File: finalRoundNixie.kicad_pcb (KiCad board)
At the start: 2 copper layers, 37 x 56.3 mm, 60 parts, among them J1 Conn_01x06_Male, J2 HV_IN, J3 Conn_01x06_Female, J4 HV_OUT, Q1 MMBTA42LT1, Q10 MMBTA42LT1, Q11 AO3400, Q12 AO3400, Q13 AO3400, Q14 MMBTA42LT1, Q15 MMBTA42LT1, Q2 MMBTA42LT1, Q3 MMBTA42LT1, Q4 MMBTA42LT1, Q5 MMBTA42LT1, Q6 MMBTA42LT1, Q7 MMBTA42LT1, Q8 MMBTA42LT1, Q9 MMBTA42LT1, U1 74HC595D, U2 nixie-tube, U3 74HC595D, U4 ams1117-5.0

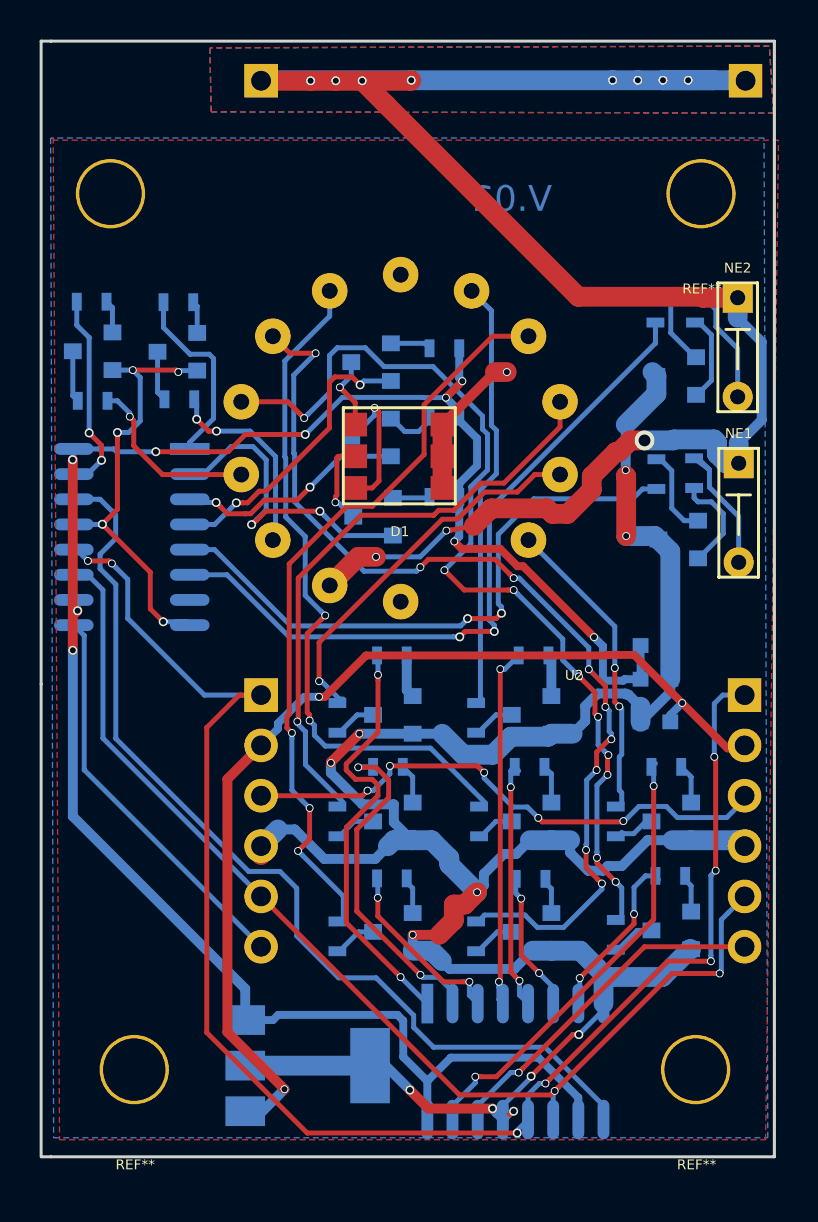
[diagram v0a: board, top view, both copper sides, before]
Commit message: changed AO3400 pin position (2 board)
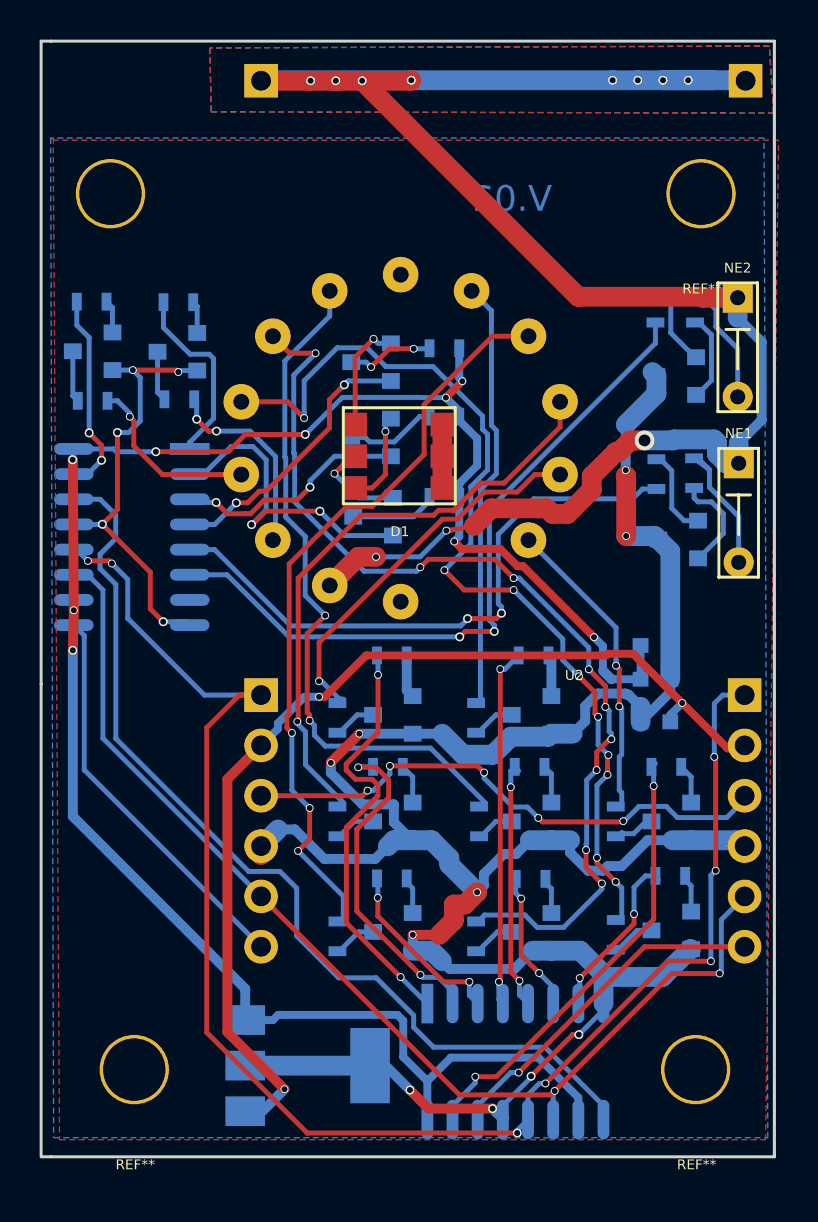
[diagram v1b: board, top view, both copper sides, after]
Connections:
- Q11 pad 1: Net-(Q11-Pad1) -> Net-(D1-Pad2)
- Q11 pad 3: Net-(D1-Pad2) -> Net-(Q11-Pad3)
- Q12 pad 1: Net-(Q12-Pad1) -> Net-(D1-Pad3)
- Q12 pad 3: Net-(D1-Pad3) -> Net-(Q12-Pad3)
- Q13 pad 1: Net-(Q13-Pad1) -> Net-(D1-Pad4)
- Q13 pad 3: Net-(D1-Pad4) -> Net-(Q13-Pad3)
- R11 pad 2: Net-(Q11-Pad1) -> Net-(Q11-Pad3)
- R12 pad 2: Net-(Q12-Pad1) -> Net-(Q12-Pad3)
- R13 pad 2: Net-(Q13-Pad1) -> Net-(Q13-Pad3)
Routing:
- net GND: track 154.6 -> 149.4 mm, vias 17 -> 15
- net Net-(Q12-Pad3): track 0.00 -> 4.62 mm
- net Net-(Q11-Pad3): track 0.00 -> 4.50 mm
- net Net-(Q13-Pad3): track 0.00 -> 4.45 mm, vias 0 -> 2
- net Net-(Q12-Pad1): track 2.65 -> 0.00 mm
- net Net-(D1-Pad3): track 7.14 -> 4.79 mm
- net Net-(Q13-Pad1): track 2.05 -> 0.00 mm
- net Net-(D1-Pad4): track 3.71 -> 5.68 mm
- net Net-(Q11-Pad1): track 1.87 -> 0.00 mm
- net /Blue: track 15.0 -> 14.2 mm
- net +5V: track 103.4 -> 102.7 mm

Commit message: remove silkscreen on female pins, re routed some of the tracks
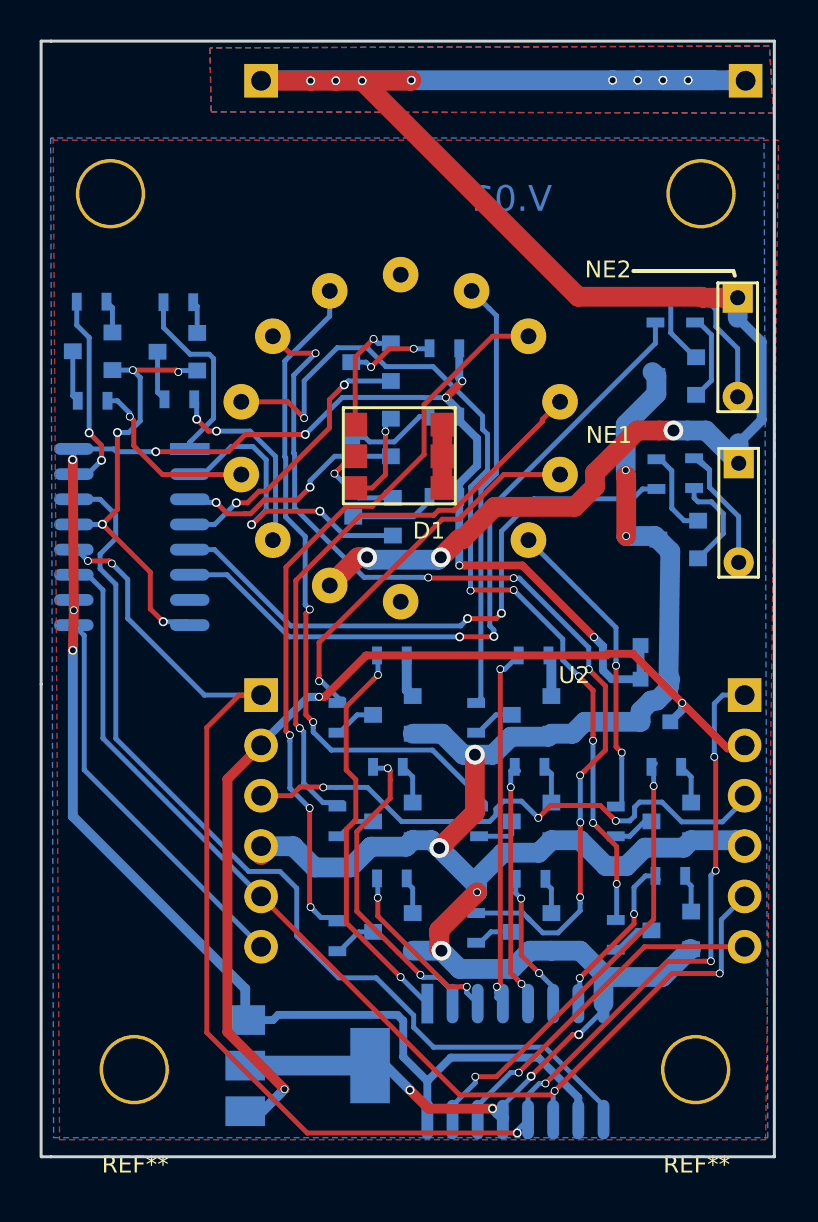
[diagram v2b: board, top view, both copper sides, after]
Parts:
- J2: footprint Socket_Strips:Socket_Strip_Angled_1x01_Pitch2.54mm -> nixie-tube-fp:Socket_Strip_Angled_1x01_Pitch2.54mm_without_silk
- J3: footprint Socket_Strips:Socket_Strip_Angled_1x06_Pitch2.54mm -> nixie-tube-fp:Socket_Strip_Angled_1x06_Pitch2.54mm_without_silk
- moved R4 0.42 mm to (173.4, 85.0)
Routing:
- net GND: track 149.4 -> 139.9 mm
- net Net-(R3-Pad1): track 48.4 -> 46.8 mm, vias 9 -> 7
- net /s1: track 21.8 -> 20.4 mm
- net /s2: track 17.2 -> 15.9 mm
- net /PWREN: track 27.6 -> 28.5 mm, vias 5 -> 3
- net /n4: track 1.58 -> 2.35 mm
- net Net-(R5-Pad1): track 34.7 -> 34.1 mm
- net Net-(R4-Pad1): track 49.6 -> 49.0 mm, vias 9 -> 7
- net /n9: track 1.79 -> 2.39 mm
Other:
- board text added: "HV"

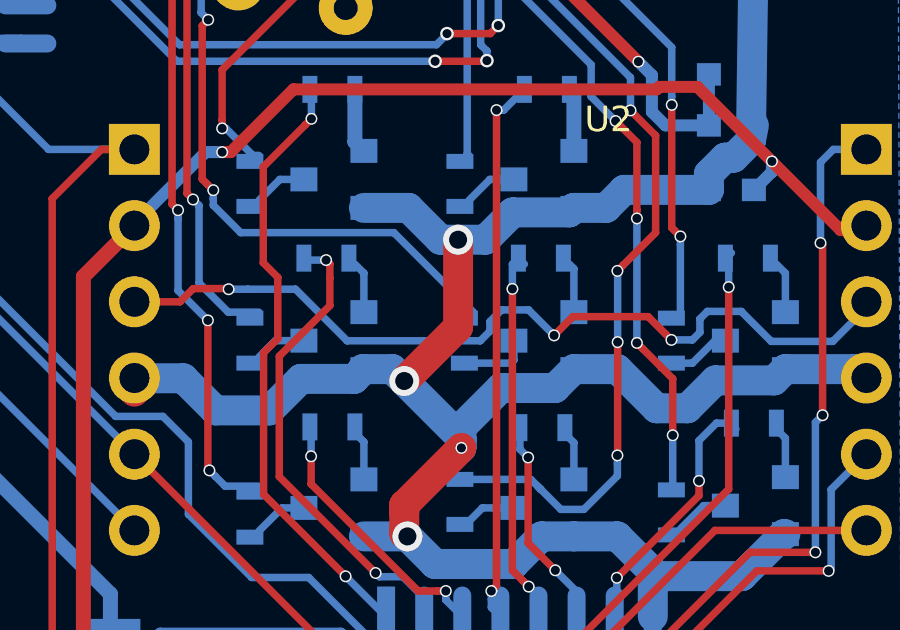
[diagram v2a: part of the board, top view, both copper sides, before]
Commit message: fixed some badly routed tracks
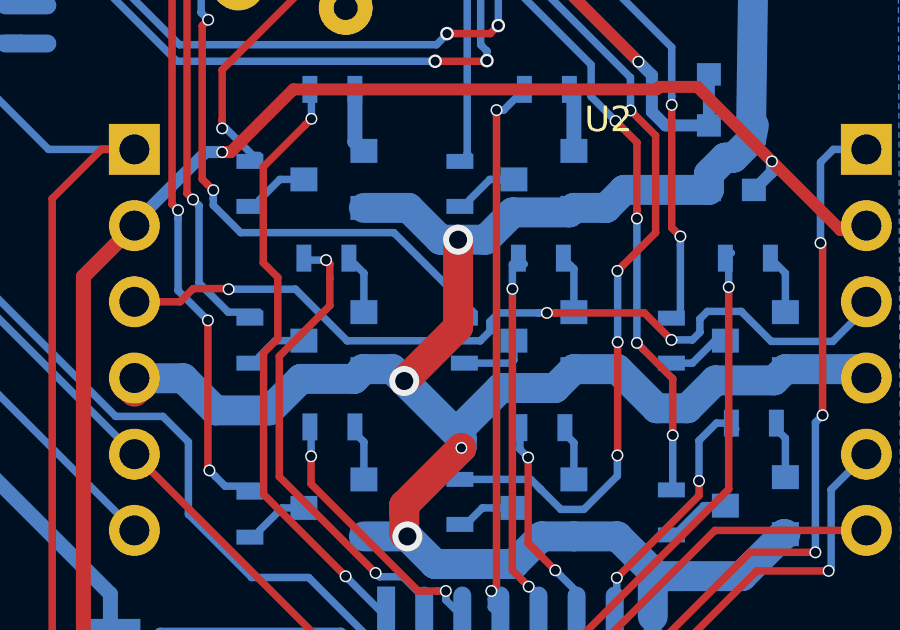
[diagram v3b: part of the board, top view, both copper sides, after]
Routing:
- net /PWREN: track 28.5 -> 27.9 mm
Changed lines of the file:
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@@
     (links 108)
     (no_connects 0)
-    (area 151.424999 40.224999 188.575001 96.675001)
+    (area 141.050001 40.224999 208.899524 100.700001)
     (thickness 1.6)
     (drawings 17)
-    (tracks 840)
+    (tracks 838)
     (zones 0)
     (modules 60)
@@
   (segment (start 185.824999 84.635001) (end 187 83.46) (width 0.25) (layer B.Cu) (net 7) (status 20))
   (via (at 185.74 87.35) (size 0.4) (drill 0.3) (layers F.Cu B.Cu) (net 7))
-  (segment (start 176.589998 79.5) (end 175.739998 78.65) (width 0.25) (layer B.Cu) (net 8))
-  (segment (start 174.45 79.360002) (end 174.130002 79.68) (width 0.25) (layer B.Cu) (net 8))
-  (segment (start 175.739998 78.65) (end 174.839998 78.65) (width 0.25) (layer B.Cu) (net 8))
-  (segment (start 174.130002 79.68) (end 169.690002 79.68) (width 0.25) (layer B.Cu) (net 8))
-  (segment (start 174.839998 78.65) (end 174.45 79.039998) (width 0.25) (layer B.Cu) (net 8))
-  (segment (start 174.45 79.039998) (end 174.45 79.360002) (width 0.25) (layer B.Cu) (net 8))
-  (segment (start 169.690002 79.68) (end 167.970002 77.96) (width 0.25) (layer B.Cu) (net 8))
-  (segment (start 167.970002 77.96) (end 166.38 77.96) (width 0.25) (layer B.Cu) (net 8))
-  (segment (start 166.38 77.96) (end 165.74 77.96) (width 0.25) (layer B.Cu) (net 8))
+  (segment (start 176.632842 78.75) (end 176.35 78.75) (width 0.25) (layer F.Cu) (net 8))
+  (segment (start 179.6 78.75) (end 176.632842 78.75) (width 0.25) (layer F.Cu) (net 8))
+  (segment (start 180.5 79.65) (end 179.6 78.75) (width 0.25) (layer F.Cu) (net 8))
+  (segment (start 176.067158 78.75) (end 176.35 78.75) (width 0.25) (layer B.Cu) (net 8))
+  (segment (start 174.45 79.360002) (end 174.45 79.039998) (width 0.25) (layer B.Cu) (net 8))
+  (segment (start 174.130002 79.68) (end 174.45 79.360002) (width 0.25) (layer B.Cu) (net 8))
+  (segment (start 169.690002 79.68) (end 174.130002 79.68) (width 0.25) (layer B.Cu) (net 8))
+  (segment (start 167.970002 77.96) (end 169.690002 79.68) (width 0.25) (layer B.Cu) (net 8))
+  (segment (start 174.739998 78.75) (end 176.067158 78.75) (width 0.25) (layer B.Cu) (net 8))
+  (segment (start 174.45 79.039998) (end 174.739998 78.75) (width 0.25) (layer B.Cu) (net 8))
+  (segment (start 165.74 77.96) (end 167.970002 77.96) (width 0.25) (layer B.Cu) (net 8))
+  (via (at 176.35 78.75) (size 0.4) (drill 0.3) (layers F.Cu B.Cu) (net 8))
   (segment (start 164.12 78.38) (end 164.56 77.94) (width 0.25) (layer F.Cu) (net 8))
   (segment (start 164.56 77.94) (end 165.72 77.94) (width 0.25) (layer F.Cu) (net 8))
@@
   (segment (start 181.45 78.95) (end 181.7 78.7) (width 0.25) (layer B.Cu) (net 8))
   (segment (start 183.827854 79.7) (end 185.88 79.7) (width 0.25) (layer B.Cu) (net 8))
-  (segment (start 180.300001 79.450001) (end 180.5 79.65) (width 0.25) (layer F.Cu) (net 8))
-  (segment (start 177.215 78.874998) (end 179.724998 78.874998) (width 0.25) (layer F.Cu) (net 8))
-  (segment (start 176.589998 79.5) (end 177.215 78.874998) (width 0.25) (layer F.Cu) (net 8))
-  (segment (start 179.724998 78.874998) (end 180.300001 79.450001) (width 0.25) (layer F.Cu) (net 8))
   (via (at 180.5 79.65) (size 0.4) (drill 0.3) (layers F.Cu B.Cu) (net 8))
-  (via (at 176.589998 79.5) (size 0.4) (drill 0.3) (layers F.Cu B.Cu) (net 8))
   (via (at 167.95 66.35) (size 1) (drill 0.6) (layers F.Cu B.Cu) (net 9))
   (segment (start 168.07 66.47) (end 171.55 66.47) (width 1) (layer B.Cu) (net 9))

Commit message: finalized every component and generated gerber file
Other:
- board text added: "GND"
- board text added: "MISO"
- board text added: "MOSI"
- board text added: "PWREN"
- board text added: "SCK"
- board text added: "STORE"
- board text added: "VDC"
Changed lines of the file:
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@@
     (area 141.050001 40.224999 208.899524 100.700001)
     (thickness 1.6)
-    (drawings 17)
+    (drawings 24)
     (tracks 838)
     (zones 0)
@@
     (40 Dwgs.User user)
     (41 Cmts.User user)
-    (42 Eco1.User user hide)
+    (42 Eco1.User user)
     (43 Eco2.User user hide)
     (44 Edge.Cuts user)
@@
     (visible_elements 7FFEFFFF)
     (pcbplotparams
-      (layerselection 0x3d4fc_80000001)
+      (layerselection 0x3d0fc_80000001)
       (usegerberextensions true)
       (usegerberattributes true)
@@
       (net 59 "Net-(NE2-Pad2)"))
   )
+  (gr_text MISO (at 168 86.25) (layer F.SilkS)
+    (effects (font (size 1.5 1.5) (thickness 0.3)))
+  )
+  (gr_text MOSI (at 181.73 86.49) (layer F.SilkS)
+    (effects (font (size 1.5 1.5) (thickness 0.3)))
+  )
+  (gr_text SCK (at 174.16 83.5) (layer F.SilkS)
+    (effects (font (size 1.5 1.5) (thickness 0.3)))
+  )
+  (gr_text GND (at 174.16 81.09) (layer F.SilkS)
+    (effects (font (size 1.5 1.5) (thickness 0.3)))
+  )
+  (gr_text PWREN (at 174.16 78.49) (layer F.SilkS)
+    (effects (font (size 1.5 1.5) (thickness 0.3)))
+  )
+  (gr_text VDC (at 174.21 75.84) (layer F.SilkS)
+    (effects (font (size 1.5 1.5) (thickness 0.3)))
+  )
+  (gr_text STORE (at 173.78 73.29) (layer F.SilkS)
+    (effects (font (size 1.5 1.5) (thickness 0.3)))
+  )
   (gr_text HV (at 174.5 42.33) (layer B.SilkS)

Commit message: finalized tracks and added symbols
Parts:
- moved R18 0.18 mm to (169.1, 77.1)
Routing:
- net GND: track 139.9 -> 177.7 mm, vias 15 -> 18
- net +5V: track 103.0 -> 122.0 mm, vias 9 -> 10
- net Net-(J2-Pad1): track 91.9 -> 86.4 mm, vias 11 -> 10
- net /SCK: track 56.3 -> 60.1 mm
- net +VDC: track 51.6 -> 54.8 mm
- net /DotU: track 30.4 -> 28.3 mm
- net Net-(R5-Pad1): track 34.1 -> 36.1 mm
- net Net-(R9-Pad1): track 19.2 -> 21.0 mm
- net Net-(R2-Pad1): track 9.34 -> 8.64 mm
- net /s8: track 10.8 -> 10.2 mm
- net Net-(R7-Pad1): track 38.1 -> 38.6 mm

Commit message: finalized everything and ready to send out
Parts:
- added Z?: skull, nixie-tube-fp:skull, F.Cu at (168.6, 42.9)
- added Z?: lightning, nixie-tube-fp:lightning, F.Cu at (182.4, 42.5)
- added Z?: skull, nixie-tube-fp:skull, B.Cu at (168.3, 42.8)
- added Z?: lightning, nixie-tube-fp:lightning, B.Cu at (182.3, 42.5)
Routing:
- net Net-(J2-Pad1): track 86.4 -> 89.1 mm

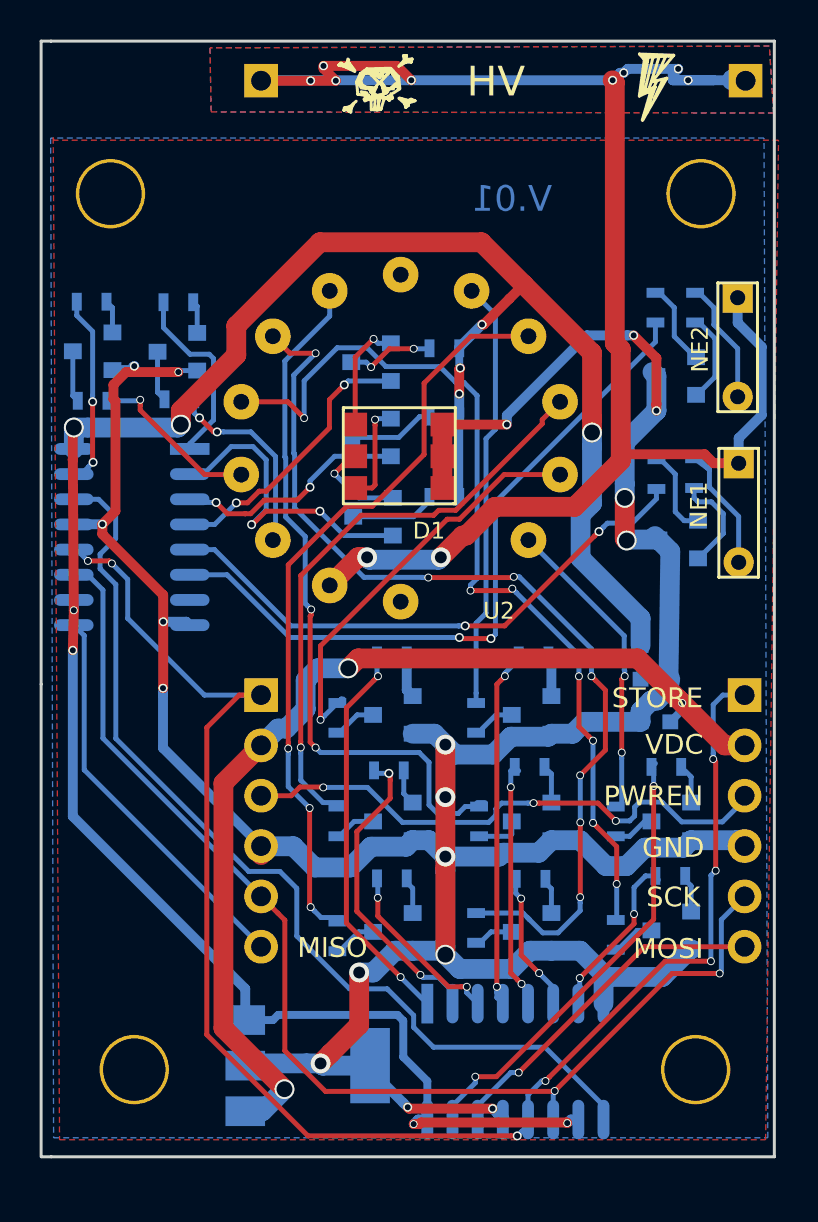
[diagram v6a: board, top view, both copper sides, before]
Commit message: fixed various bugs
RGB led not connected properly to the mosfet
AO3400 pin orientation is not same with datasheet
move silkscreen away on neon footprint
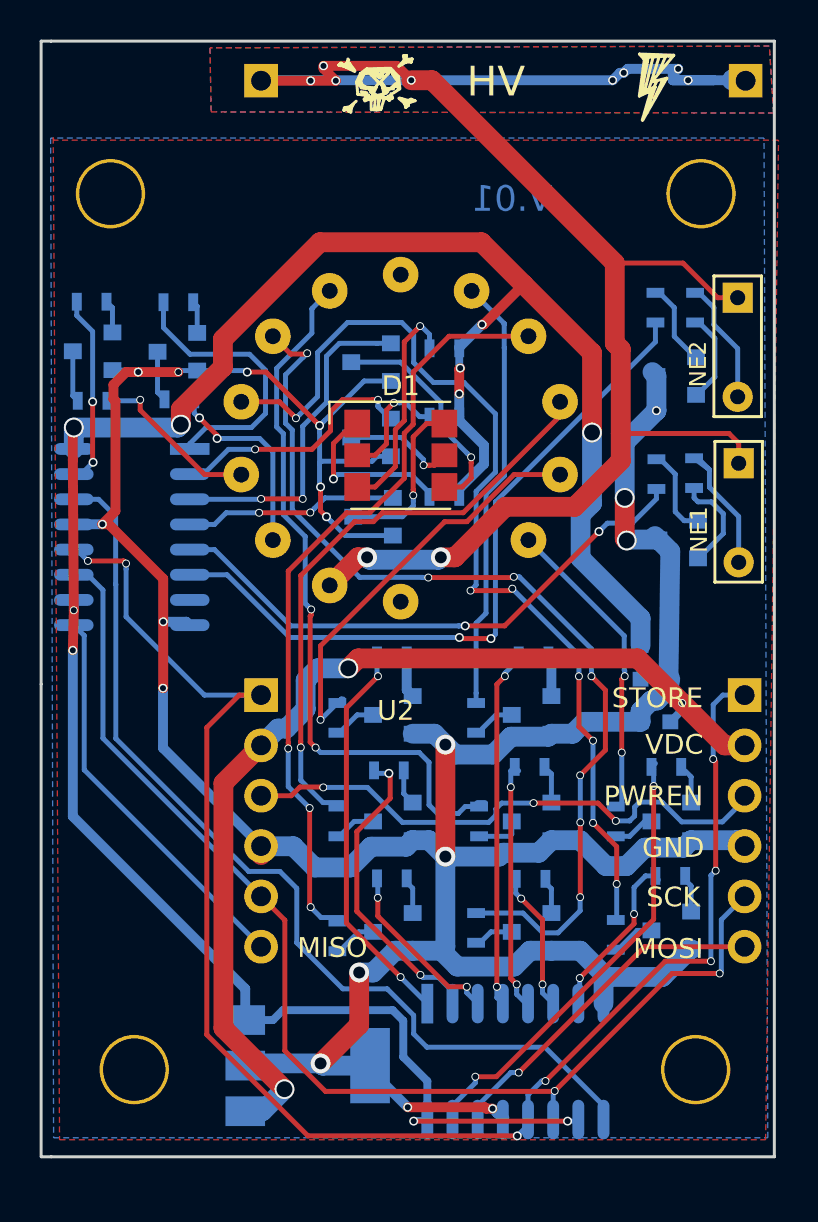
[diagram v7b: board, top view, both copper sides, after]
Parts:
- D1: value LED_CRGB -> LED_RGB_BGR; footprint nixie-tube-fp:Rgb-Led -> nixie-tube-fp:LED_RGB_5050-6
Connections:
- D1 pad 1: GND -> Net-(D1-Pad1)
- Q11 pad 1: Net-(D1-Pad2) -> /Blue
- Q11 pad 2: /Red -> GND
- Q11 pad 3: Net-(Q11-Pad3) -> Net-(D1-Pad6)
- Q12 pad 1: Net-(D1-Pad3) -> /Red
- Q12 pad 2: /Green -> GND
- Q12 pad 3: Net-(Q12-Pad3) -> Net-(D1-Pad5)
- Q13 pad 1: Net-(D1-Pad4) -> /Green
- Q13 pad 2: /Blue -> GND
- Q13 pad 3: Net-(Q13-Pad3) -> Net-(D1-Pad4)
- R11 pad 2: Net-(Q11-Pad3) -> Net-(D1-Pad1)
- R12 pad 2: Net-(Q12-Pad3) -> Net-(D1-Pad2)
- R13 pad 2: Net-(Q13-Pad3) -> Net-(D1-Pad3)
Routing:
- net Net-(D1-Pad1): track 0.00 -> 9.13 mm, vias 0 -> 1
- net Net-(D1-Pad6): track 0.00 -> 8.64 mm, vias 0 -> 1
- net Net-(D1-Pad3): track 5.23 -> 11.5 mm
- net Net-(D1-Pad4): track 5.68 -> 11.6 mm
- net Net-(D1-Pad5): track 0.00 -> 5.89 mm, vias 0 -> 1
- net /Green: track 11.8 -> 17.3 mm
- net /s9: track 9.52 -> 14.2 mm
- net Net-(Q11-Pad3): track 4.50 -> 0.00 mm
- net Net-(Q13-Pad3): track 4.45 -> 0.00 mm, vias 2 -> 0
- net Net-(Q12-Pad3): track 4.43 -> 0.00 mm
- net /Blue: track 14.2 -> 10.8 mm
- net /Red: track 16.3 -> 12.9 mm
- net Net-(J2-Pad1): track 89.1 -> 92.4 mm
- net Net-(R3-Pad1): track 46.9 -> 49.7 mm
- net +VDC: track 54.8 -> 52.3 mm
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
